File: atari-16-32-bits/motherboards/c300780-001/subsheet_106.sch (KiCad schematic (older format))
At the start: 47 parts, among them Q100 2N3904, Q101 2N3904, Q102 2N3904, Q103 2N3904, Q104 2N3904, U402 32.215905 MHz (NTSC) — 32.084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, Y100 4.433618MHz, Y101 32.084988MHz

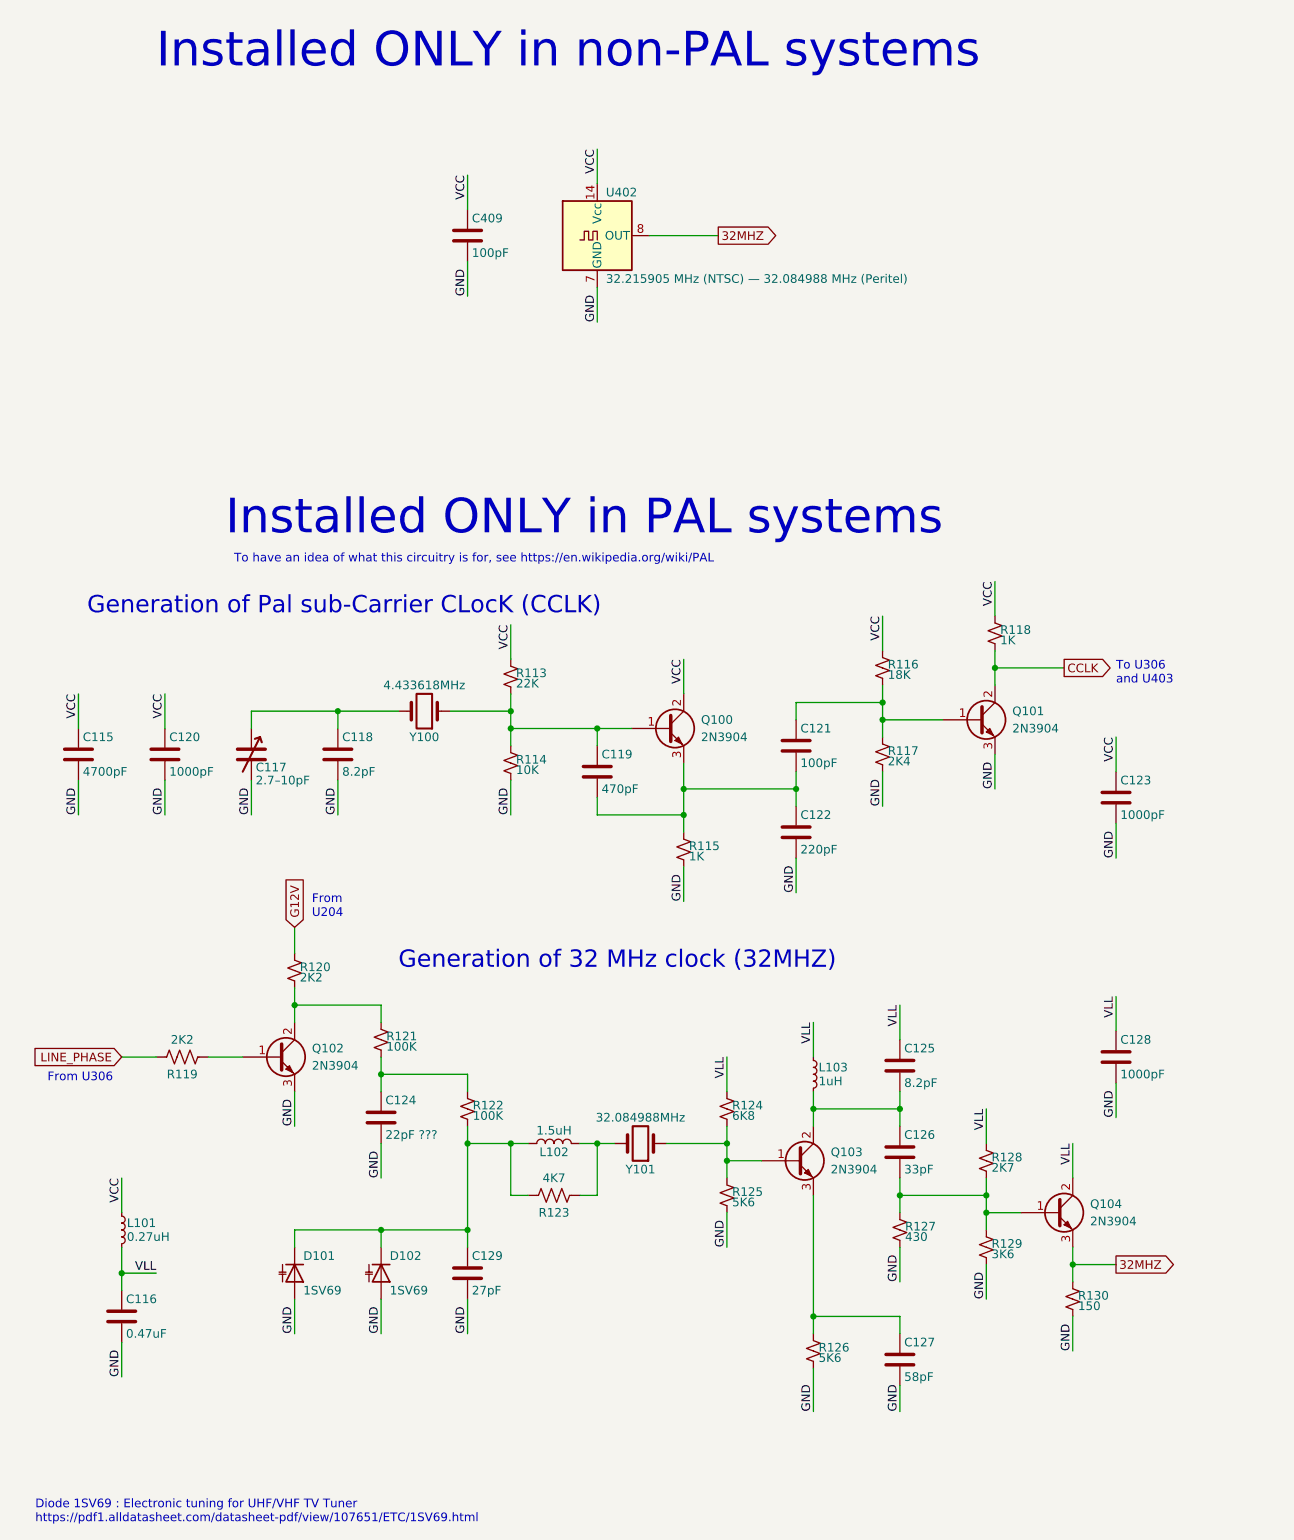
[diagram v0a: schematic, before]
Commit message: Fixes #10 : [Atari STE] R126 should be 560 R
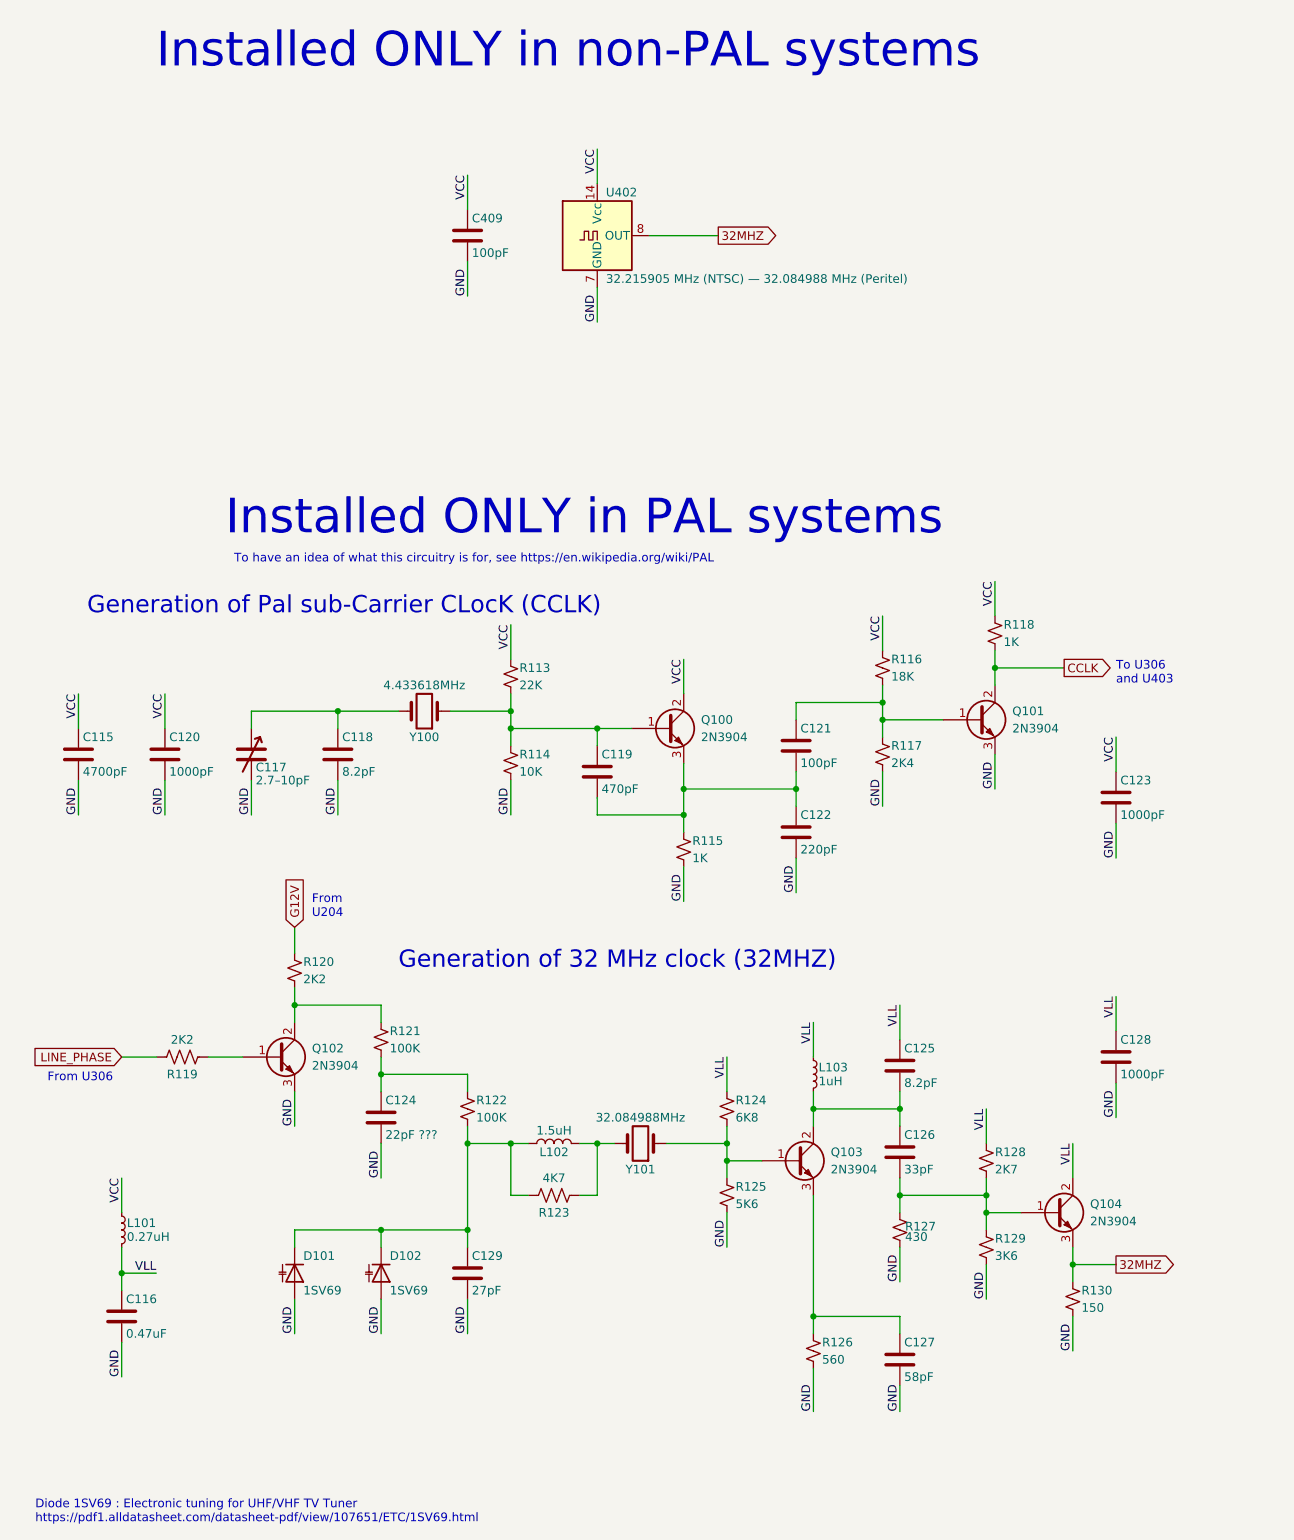
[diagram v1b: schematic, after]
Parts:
- R126: value 5K6 -> 560
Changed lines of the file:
@@
 U 1 1 6086B8E5
 P 3500 4800
-F 0 "R113" H 3530 4820 50  0000 L CNN
-F 1 "22K" H 3530 4760 50  0000 L CNN
+F 0 "R113" H 3550 4850 50  0000 L CNN
+F 1 "22K" H 3550 4750 50  0000 L CNN
 F 2 "" H 3500 4800 50  0001 C CNN
 F 3 "~" H 3500 4800 50  0001 C CNN
@@
 U 1 1 6086BB82
 P 3500 5300
-F 0 "R114" H 3530 5320 50  0000 L CNN
-F 1 "10K" H 3530 5260 50  0000 L CNN
+F 0 "R114" H 3550 5350 50  0000 L CNN
+F 1 "10K" H 3550 5250 50  0000 L CNN
 F 2 "" H 3500 5300 50  0001 C CNN
 F 3 "~" H 3500 5300 50  0001 C CNN
@@
 U 1 1 6086CF8D
 P 5650 4750
-F 0 "R116" H 5680 4770 50  0000 L CNN
-F 1 "18K" H 5680 4710 50  0000 L CNN
+F 0 "R116" H 5700 4800 50  0000 L CNN
+F 1 "18K" H 5700 4700 50  0000 L CNN
 F 2 "" H 5650 4750 50  0001 C CNN
 F 3 "~" H 5650 4750 50  0001 C CNN
@@
 U 1 1 6086CF94
 P 5650 5250
-F 0 "R117" H 5680 5270 50  0000 L CNN
-F 1 "2K4" H 5680 5210 50  0000 L CNN
+F 0 "R117" H 5700 5300 50  0000 L CNN
+F 1 "2K4" H 5700 5200 50  0000 L CNN
 F 2 "" H 5650 5250 50  0001 C CNN
 F 3 "~" H 5650 5250 50  0001 C CNN
@@
 U 1 1 60875D86
 P 4500 5800
-F 0 "R115" H 4530 5820 50  0000 L CNN
-F 1 "1K" H 4530 5760 50  0000 L CNN
+F 0 "R115" H 4550 5850 50  0000 L CNN
+F 1 "1K" H 4550 5750 50  0000 L CNN
 F 2 "" H 4500 5800 50  0001 C CNN
 F 3 "~" H 4500 5800 50  0001 C CNN
@@
 U 1 1 60883C2D
 P 6300 4550
-F 0 "R118" H 6330 4570 50  0000 L CNN
-F 1 "1K" H 6330 4510 50  0000 L CNN
+F 0 "R118" H 6350 4600 50  0000 L CNN
+F 1 "1K" H 6350 4500 50  0000 L CNN
 F 2 "" H 6300 4550 50  0001 C CNN
 F 3 "~" H 6300 4550 50  0001 C CNN
@@
 U 1 1 608A0CAB
 P 2250 6500
-F 0 "R120" H 2280 6520 50  0000 L CNN
-F 1 "2K2" H 2280 6460 50  0000 L CNN
+F 0 "R120" H 2300 6550 50  0000 L CNN
+F 1 "2K2" H 2300 6450 50  0000 L CNN
 F 2 "" H 2250 6500 50  0001 C CNN
 F 3 "~" H 2250 6500 50  0001 C CNN
@@
 U 1 1 608A66AB
 P 2750 6900
-F 0 "R121" H 2780 6920 50  0000 L CNN
-F 1 "100K" H 2780 6860 50  0000 L CNN
+F 0 "R121" H 2800 6950 50  0000 L CNN
+F 1 "100K" H 2800 6850 50  0000 L CNN
 F 2 "" H 2750 6900 50  0001 C CNN
 F 3 "~" H 2750 6900 50  0001 C CNN
@@
 U 1 1 608AF033
 P 3250 7300
-F 0 "R122" H 3280 7320 50  0000 L CNN
-F 1 "100K" H 3280 7260 50  0000 L CNN
+F 0 "R122" H 3300 7350 50  0000 L CNN
+F 1 "100K" H 3300 7250 50  0000 L CNN
 F 2 "" H 3250 7300 50  0001 C CNN
 F 3 "~" H 3250 7300 50  0001 C CNN
@@
 U 1 1 608D7B0F
 P 4750 7300
-F 0 "R124" H 4780 7320 50  0000 L CNN
-F 1 "6K8" H 4780 7260 50  0000 L CNN
+F 0 "R124" H 4800 7350 50  0000 L CNN
+F 1 "6K8" H 4800 7250 50  0000 L CNN
 F 2 "" H 4750 7300 50  0001 C CNN
 F 3 "~" H 4750 7300 50  0001 C CNN
@@
 U 1 1 608D7B15
 P 4750 7800
-F 0 "R125" H 4780 7820 50  0000 L CNN
-F 1 "5K6" H 4780 7760 50  0000 L CNN
+F 0 "R125" H 4800 7850 50  0000 L CNN
+F 1 "5K6" H 4800 7750 50  0000 L CNN
 F 2 "" H 4750 7800 50  0001 C CNN
 F 3 "~" H 4750 7800 50  0001 C CNN
@@
 U 1 1 608E45AA
 P 5250 8700
-F 0 "R126" H 5280 8720 50  0000 L CNN
-F 1 "5K6" H 5280 8660 50  0000 L CNN
+F 0 "R126" H 5300 8750 50  0000 L CNN
+F 1 "560" H 5300 8650 50  0000 L CNN
 F 2 "" H 5250 8700 50  0001 C CNN
 F 3 "~" H 5250 8700 50  0001 C CNN
@@
 U 1 1 60933AC1
 P 6250 7600
-F 0 "R128" H 6280 7620 50  0000 L CNN
-F 1 "2K7" H 6280 7560 50  0000 L CNN
+F 0 "R128" H 6300 7650 50  0000 L CNN
+F 1 "2K7" H 6300 7550 50  0000 L CNN
 F 2 "" H 6250 7600 50  0001 C CNN
 F 3 "~" H 6250 7600 50  0001 C CNN
@@
 U 1 1 60934947
 P 6250 8100
-F 0 "R129" H 6280 8120 50  0000 L CNN
-F 1 "3K6" H 6280 8060 50  0000 L CNN
+F 0 "R129" H 6300 8150 50  0000 L CNN
+F 1 "3K6" H 6300 8050 50  0000 L CNN
 F 2 "" H 6250 8100 50  0001 C CNN
 F 3 "~" H 6250 8100 50  0001 C CNN
@@
 U 1 1 609372ED
 P 6750 8400
-F 0 "R130" H 6780 8420 50  0000 L CNN
-F 1 "150" H 6780 8360 50  0000 L CNN
+F 0 "R130" H 6800 8450 50  0000 L CNN
+F 1 "150" H 6800 8350 50  0000 L CNN
 F 2 "" H 6750 8400 50  0001 C CNN
 F 3 "~" H 6750 8400 50  0001 C CNN

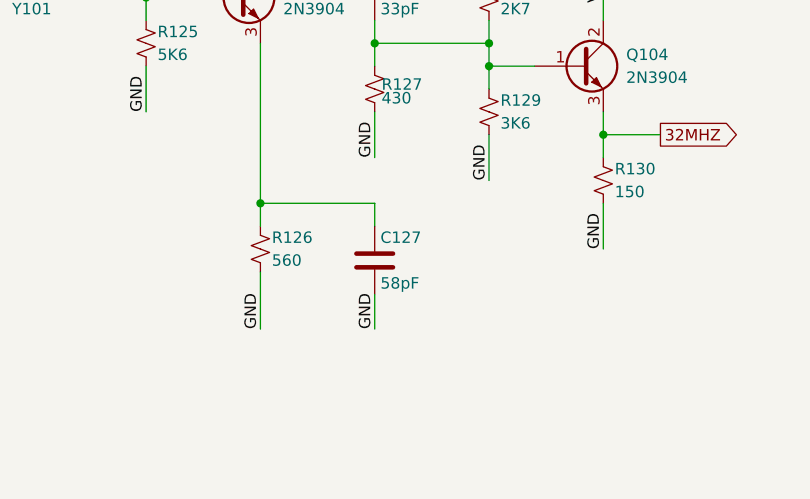
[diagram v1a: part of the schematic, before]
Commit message: Fixes #11 : [Atari STE] C127 should be 68 pF
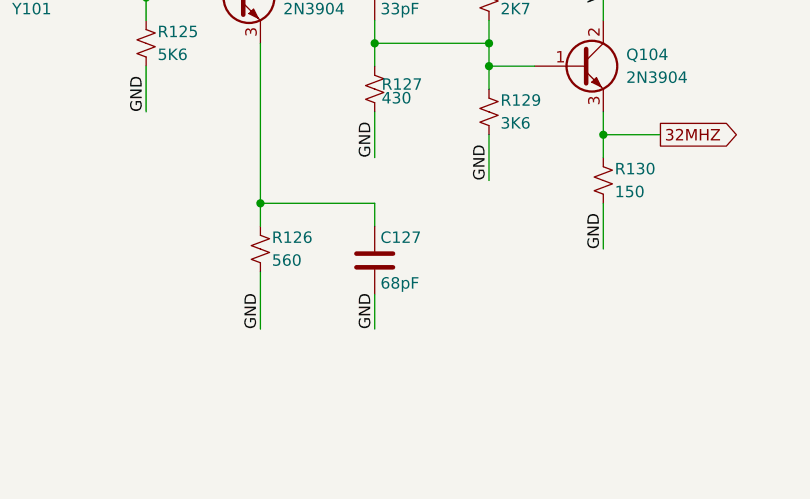
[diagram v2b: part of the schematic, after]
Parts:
- C127: value 58pF -> 68pF
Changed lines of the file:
@@
 P 5750 8750
 F 0 "C127" H 5775 8850 50  0000 L CNN
-F 1 "58pF" H 5775 8650 50  0000 L CNN
+F 1 "68pF" H 5775 8650 50  0000 L CNN
 F 2 "" H 5788 8600 50  0001 C CNN
 F 3 "~" H 5750 8750 50  0001 C CNN

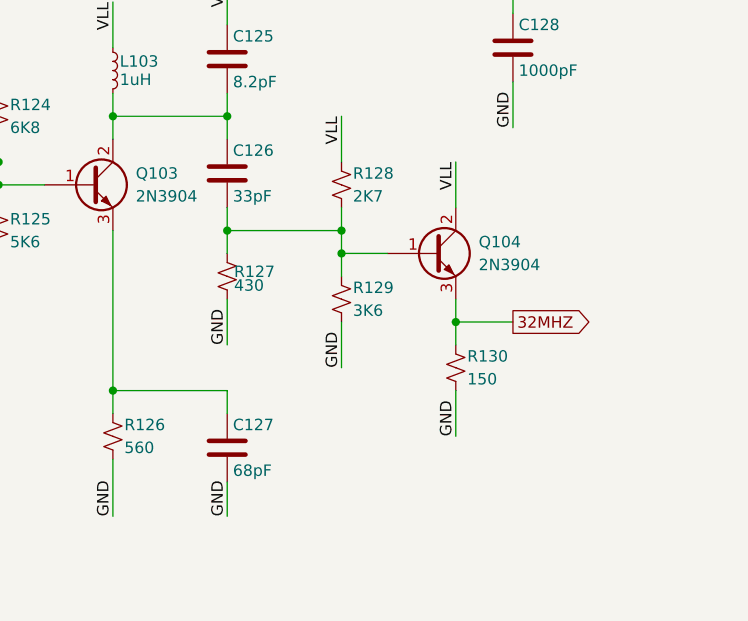
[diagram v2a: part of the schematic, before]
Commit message: Fixes #12 : [Atari STE] R127 does not go to ground
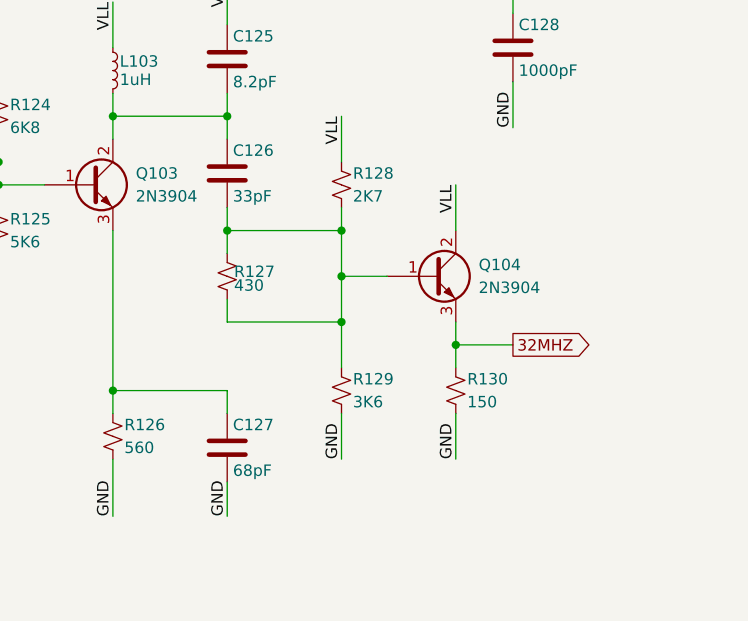
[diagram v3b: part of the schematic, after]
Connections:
- net GND: no longer R127.2
- net at C126.2, Q104.1 (B), R127.1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: now also R127.2
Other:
- moved on the sheet: Q104, R129, R130
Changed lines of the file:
@@
 Text Label 5750 6700 3    50   ~ 0
 VLL
-Text Label 5750 8300 1    50   ~ 0
-GND
 $Comp
 L Device:R_Small_US R128
@@
 L Device:R_Small_US R129
 U 1 1 60934947
-P 6250 8100
-F 0 "R129" H 6300 8150 50  0000 L CNN
-F 1 "3K6" H 6300 8050 50  0000 L CNN
-F 2 "" H 6250 8100 50  0001 C CNN
-F 3 "~" H 6250 8100 50  0001 C CNN
-	1    6250 8100
+P 6250 8500
+F 0 "R129" H 6300 8550 50  0000 L CNN
+F 1 "3K6" H 6300 8450 50  0000 L CNN
+F 2 "" H 6250 8500 50  0001 C CNN
+F 3 "~" H 6250 8500 50  0001 C CNN
+	1    6250 8500
 	1    0    0    -1
 $EndComp
@@
 L Device:Q_NPN_BCE Q104
 U 1 1 6093547F
-P 6650 7900
-F 0 "Q104" H 6850 7950 50  0000 L CNN
-F 1 "2N3904" H 6850 7850 50  0000 L CNN
-F 2 "" H 6850 8000 50  0001 C CNN
-F 3 "~" H 6650 7900 50  0001 C CNN
-	1    6650 7900
+P 6650 8000
+F 0 "Q104" H 6850 8050 50  0000 L CNN
+F 1 "2N3904" H 6850 7950 50  0000 L CNN
+F 2 "" H 6850 8100 50  0001 C CNN
+F 3 "~" H 6650 8000 50  0001 C CNN
+	1    6650 8000
 	1    0    0    -1
 $EndComp
 Text Label 6250 7300 3    50   ~ 0
 VLL
-Text Label 6750 7500 3    50   ~ 0
+Text Label 6750 7600 3    50   ~ 0
 VLL
-Text Label 6250 8400 1    50   ~ 0
+Text Label 6250 8800 1    50   ~ 0
 GND
-Text Label 6750 8700 1    50   ~ 0
+Text Label 6750 8800 1    50   ~ 0
 GND
 $Comp
 L Device:R_Small_US R130
 U 1 1 609372ED
-P 6750 8400
-F 0 "R130" H 6800 8450 50  0000 L CNN
-F 1 "150" H 6800 8350 50  0000 L CNN
-F 2 "" H 6750 8400 50  0001 C CNN
-F 3 "~" H 6750 8400 50  0001 C CNN
-	1    6750 8400
+P 6750 8500
+F 0 "R130" H 6800 8550 50  0000 L CNN
+F 1 "150" H 6800 8450 50  0000 L CNN
+F 2 "" H 6750 8500 50  0001 C CNN
+F 3 "~" H 6750 8500 50  0001 C CNN
+	1    6750 8500
 	1    0    0    -1
 $EndComp
-Text GLabel 7000 8200 2    50   Output ~ 0
+Text GLabel 7000 8300 2    50   Output ~ 0
 32MHZ
 Wire Wire Line
@@
 	5750 7700 5750 7800
 Wire Wire Line
-	5750 8100 5750 8300
+	5750 8100 5750 8200
 Wire Wire Line
 	6250 7300 6250 7500
@@
 Connection ~ 6250 7800
 Wire Wire Line
-	6250 7800 6250 7900
+	6250 8000 6450 8000
 Wire Wire Line
-	6250 7900 6450 7900
-Connection ~ 6250 7900
-Wire Wire Line
-	6250 7900 6250 8000
-Wire Wire Line
-	6750 7500 6750 7700
-Wire Wire Line
-	6750 8100 6750 8200
-Wire Wire Line
-	6250 8200 6250 8400
-Wire Wire Line
-	6750 8500 6750 8700
-Wire Wire Line
-	6750 8200 7000 8200
-Connection ~ 6750 8200
+	6750 7600 6750 7800
 Wire Wire Line
 	6750 8200 6750 8300
+Wire Wire Line
+	6250 8600 6250 8800
+Wire Wire Line
+	6750 8600 6750 8800
+Wire Wire Line
+	6750 8300 7000 8300
+Connection ~ 6750 8300
+Wire Wire Line
+	6750 8300 6750 8400
 Wire Wire Line
 	5250 7300 5750 7300
@@
 Text Notes 750  9700 0    50   ~ 0
 Diode 1SV69 : Electronic tuning for UHF/VHF TV Tuner\nhttps://pdf1.alldatasheet.com/datasheet-pdf/view/107651/ETC/1SV69.html
+Wire Wire Line
+	5750 8200 6250 8200
+Connection ~ 6250 8200
+Wire Wire Line
+	6250 8200 6250 8400
+Connection ~ 6250 8000
+Wire Wire Line
+	6250 8000 6250 8200
+Wire Wire Line
+	6250 7800 6250 8000
 $EndSCHEMATC

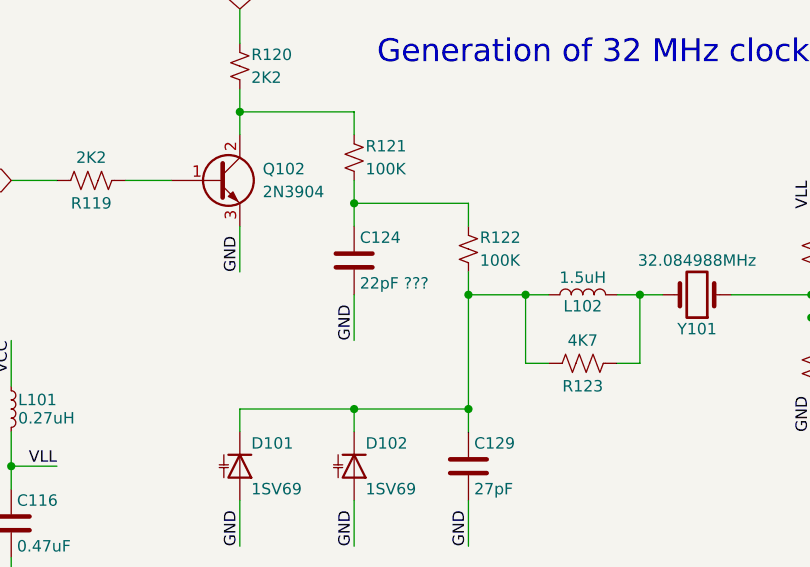
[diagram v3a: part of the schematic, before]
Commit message: Fixed : C124 is 22nF
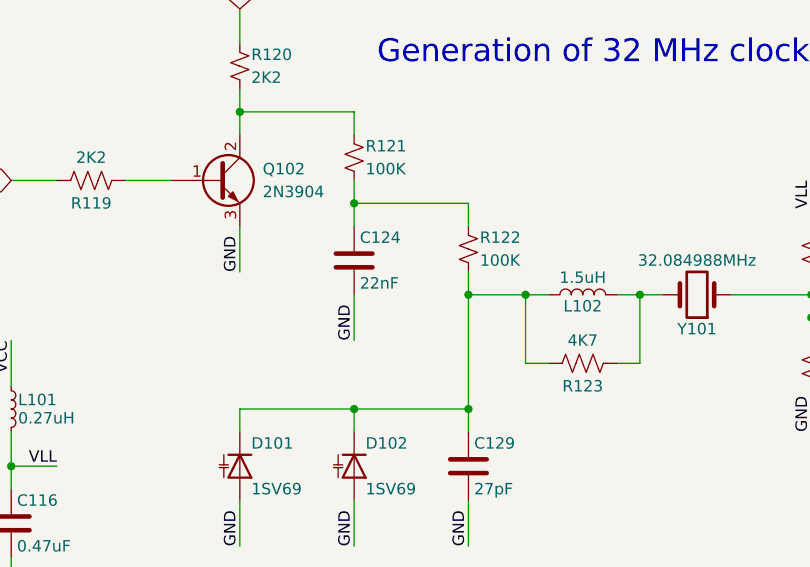
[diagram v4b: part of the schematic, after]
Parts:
- C124: value 22pF ??? -> 22nF
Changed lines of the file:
@@
 P 2750 7350
 F 0 "C124" H 2775 7450 50  0000 L CNN
-F 1 "22pF ???" H 2775 7250 50  0000 L CNN
+F 1 "22nF" H 2775 7250 50  0000 L CNN
 F 2 "" H 2788 7200 50  0001 C CNN
 F 3 "~" H 2750 7350 50  0001 C CNN
